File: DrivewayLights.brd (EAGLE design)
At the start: 69.8 x 83.8 mm, 36 parts, among them U1 TLC59108PW

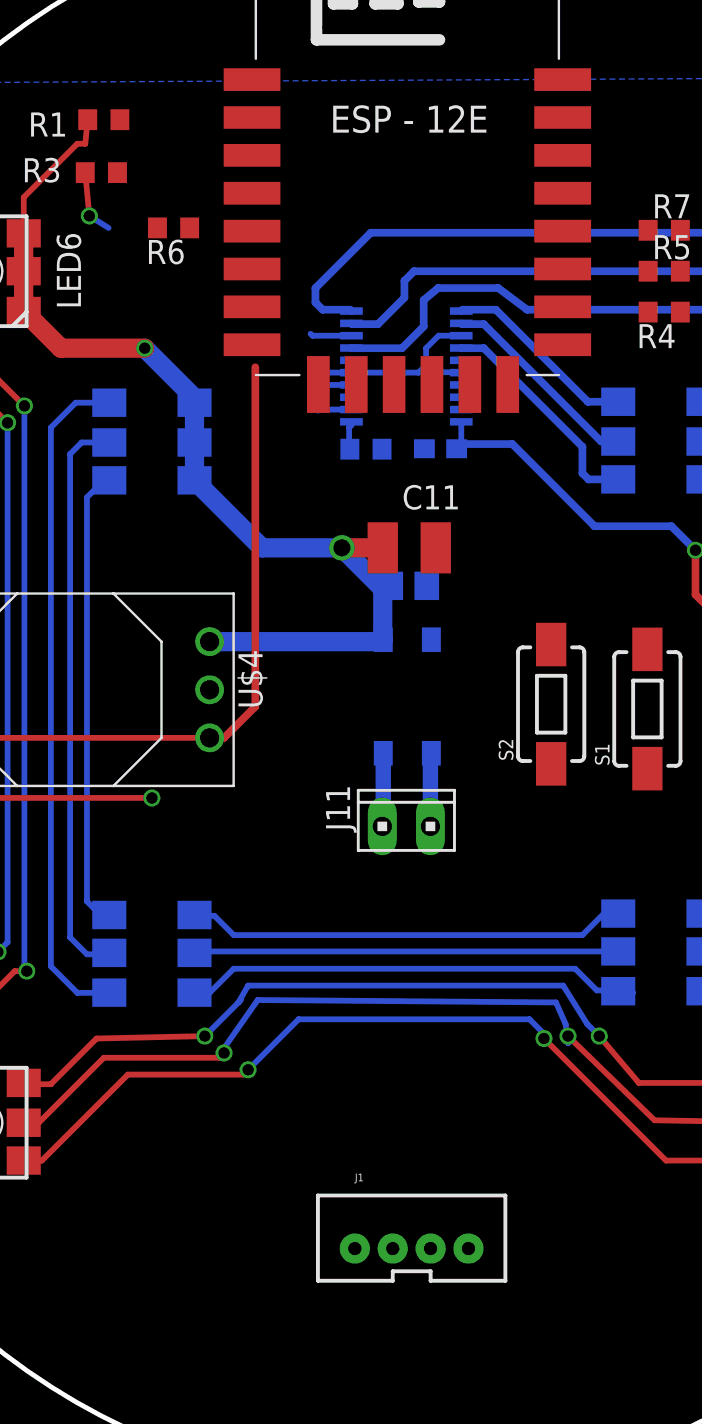
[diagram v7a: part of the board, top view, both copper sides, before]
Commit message: Added some missing connections on schematic and did some more manual routing
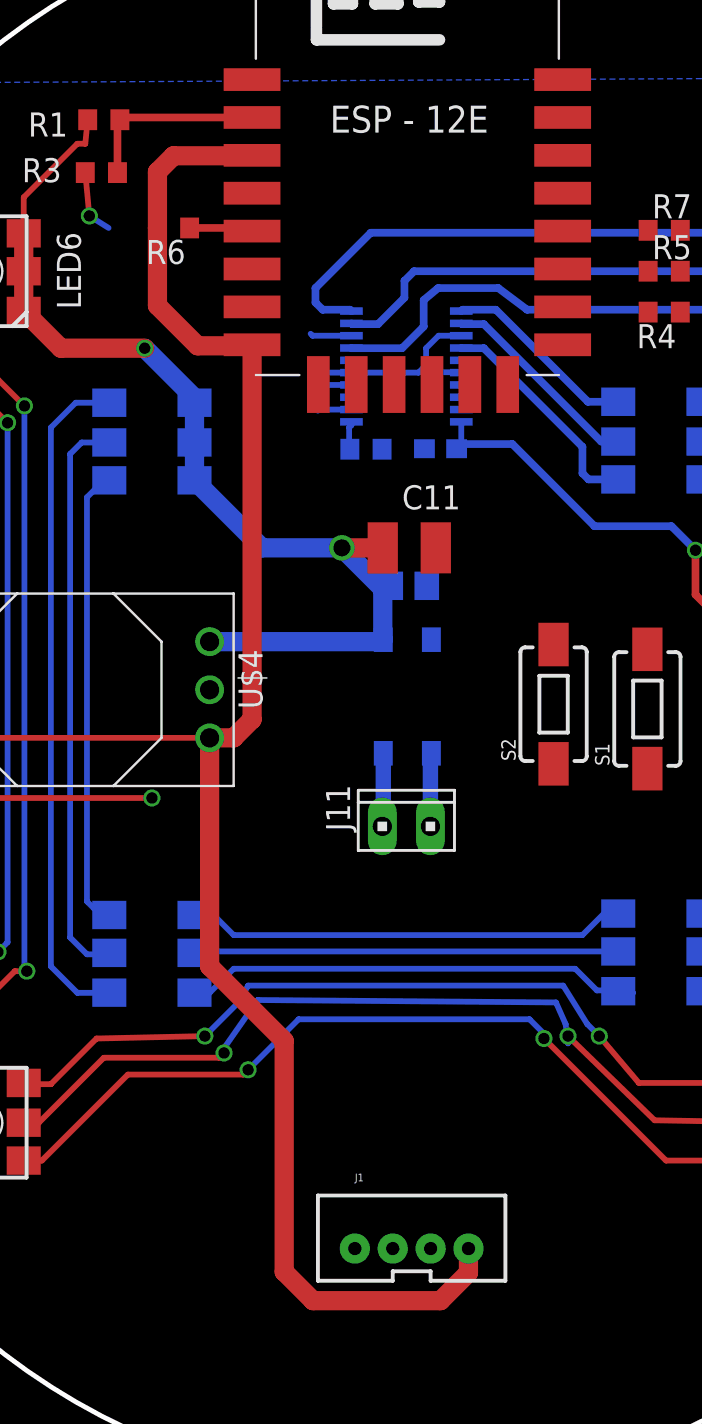
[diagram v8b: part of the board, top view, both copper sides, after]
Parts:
- moved S2 0.13 mm to (42.7, 41.5)
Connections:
- net FLASH_N: now also S1.1
- net GND: now also S1.2, S2.2
- net LED_NRESET: now also U3.GPIO16
- net RESET_N: now also S2.1
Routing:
- net 3.3V: track 105.3 -> 167.1 mm
- net ADC: track 0.00 -> 10.0 mm
- net LED_SCL: track 0.00 -> 3.46 mm
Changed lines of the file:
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@@
 <attribute name="PROD_ID" value="SWCH-00815" x="47.625" y="41.275" size="1.778" layer="27" rot="R90" display="off"/>
 </element>
-<element name="S2" library="SparkFun-Electromechanical" package="TACTILE-SWITCH-1101NE" value="SWITCH-MOMENTARY-2SMD-1101NE" x="42.545" y="41.529" rot="R90">
-<attribute name="PROD_ID" value="SWCH-00815" x="42.545" y="41.529" size="1.778" layer="27" rot="R90" display="off"/>
+<element name="S2" library="SparkFun-Electromechanical" package="TACTILE-SWITCH-1101NE" value="SWITCH-MOMENTARY-2SMD-1101NE" x="42.672" y="41.529" rot="R90">
+<attribute name="PROD_ID" value="SWCH-00815" x="42.672" y="41.529" size="1.778" layer="27" rot="R90" display="off"/>
 </element>
 <element name="J1" library="SparkFun-Connectors" package="JST-4-PTH-VERT" value="" x="35.179" y="13.335">
@@
 <contactref element="R4" pad="1"/>
 <contactref element="J1" pad="1"/>
+<contactref element="S2" pad="2"/>
+<contactref element="S1" pad="2"/>
 <wire x1="43.152" y1="60.507" x2="49.364" y2="62.23" width="0" layer="19" extent="1-1"/>
 <wire x1="37.7996" y1="60.9848" x2="43.152" y2="60.507" width="0" layer="19" extent="1-16"/>
@@
 <wire x1="31.9996" y1="57.0848" x2="31.9996" y2="57.7348" width="0" layer="19" extent="16-16"/>
 <wire x1="29.9472" y1="60.9848" x2="29.972" y2="59.055" width="0" layer="19" extent="16-16"/>
-<wire x1="36.452" y1="49.784" x2="35.9766" y2="47.7774" width="0" layer="19" extent="1-16"/>
+<wire x1="33.616" y1="54.991" x2="31.9996" y2="57.0848" width="0" layer="19" extent="16-16"/>
+<wire x1="35.853" y1="55.0164" x2="33.616" y2="54.991" width="0" layer="19" extent="16-16"/>
+<wire x1="36.452" y1="49.784" x2="35.853" y2="55.0164" width="0" layer="19" extent="1-16"/>
+<wire x1="35.9766" y1="47.7774" x2="36.452" y2="49.784" width="0" layer="19" extent="1-16"/>
+<wire x1="36.2204" y1="44.9354" x2="35.9766" y2="47.7774" width="0" layer="19" extent="16-16"/>
+<wire x1="42.672" y1="44.679" x2="36.2204" y2="44.9354" width="0" layer="19" extent="1-16"/>
+<wire x1="47.625" y1="44.425" x2="42.672" y2="44.679" width="0" layer="19" extent="1-1"/>
+<wire x1="59.436" y1="44.069" x2="47.625" y2="44.425" width="0" layer="19" extent="1-16"/>
+<wire x1="24.511" y1="42.291" x2="36.2204" y2="44.9354" width="0" layer="19" extent="16-16"/>
+<wire x1="21.463" y1="36.576" x2="24.511" y2="42.291" width="0" layer="19" extent="1-1"/>
+<wire x1="19.177" y1="66.675" x2="29.845" y2="61.087" width="0" layer="19" extent="16-16"/>
+<wire x1="32.179" y1="12.785" x2="21.463" y2="36.576" width="0" layer="19" extent="1-1"/>
 </signal>
 <signal name="3.3V">
@@
 <contactref element="IR1A" pad="A"/>
 <contactref element="IR2A" pad="A"/>
-<wire x1="24.511" y1="39.751" x2="25.273" y2="39.751" width="0.4064" layer="1"/>
-<wire x1="25.273" y1="39.751" x2="26.924" y2="41.402" width="0.4064" layer="1"/>
-<wire x1="26.924" y1="41.402" x2="26.924" y2="59.319" width="0.4064" layer="1"/>
 <wire x1="37.7996" y1="56.4348" x2="37.7996" y2="55.263" width="0.3048" layer="16"/>
 <wire x1="37.7996" y1="55.263" x2="37.553" y2="55.0164" width="0.3048" layer="16"/>
@@
 <contactref element="R6" pad="2"/>
 <contactref element="J1" pad="4"/>
+<wire x1="24.511" y1="39.751" x2="24.511" y2="27.686" width="1.016" layer="1"/>
+<wire x1="24.511" y1="27.686" x2="28.448" y2="23.749" width="1.016" layer="1"/>
+<wire x1="28.448" y1="23.749" x2="28.448" y2="11.557" width="1.016" layer="1"/>
+<wire x1="28.448" y1="11.557" x2="29.972" y2="10.033" width="1.016" layer="1"/>
+<wire x1="29.972" y1="10.033" x2="36.703" y2="10.033" width="1.016" layer="1"/>
+<wire x1="36.703" y1="10.033" x2="38.179" y2="11.509" width="1.016" layer="1"/>
+<wire x1="38.179" y1="11.509" x2="38.179" y2="12.785" width="1.016" layer="1"/>
+<wire x1="24.511" y1="39.751" x2="25.781" y2="39.751" width="1.016" layer="1"/>
+<wire x1="25.781" y1="39.751" x2="26.752" y2="40.722" width="1.016" layer="1"/>
+<wire x1="26.752" y1="40.722" x2="26.752" y2="60.507" width="1.016" layer="1"/>
+<wire x1="26.752" y1="60.507" x2="26.697" y2="60.452" width="1.016" layer="1"/>
+<wire x1="26.697" y1="60.452" x2="23.876" y2="60.452" width="1.016" layer="1"/>
+<wire x1="23.876" y1="60.452" x2="21.756" y2="62.572" width="1.016" layer="1"/>
+<wire x1="21.756" y1="62.572" x2="21.756" y2="66.675" width="1.016" layer="1"/>
+<wire x1="26.752" y1="70.507" x2="26.73" y2="70.485" width="1.016" layer="1"/>
+<wire x1="26.73" y1="70.485" x2="22.606" y2="70.485" width="1.016" layer="1"/>
+<wire x1="22.606" y1="70.485" x2="21.756" y2="69.635" width="1.016" layer="1"/>
+<wire x1="21.756" y1="69.635" x2="21.756" y2="66.675" width="1.016" layer="1"/>
 <wire x1="49.364" y1="64.389" x2="49.364" y2="66.548" width="0" layer="19" extent="1-1"/>
 <wire x1="40.495" y1="55.263" x2="49.364" y2="64.389" width="0" layer="19" extent="1-16"/>
-<wire x1="26.924" y1="59.319" x2="37.7996" y2="56.4348" width="0" layer="19" extent="1-16"/>
-<wire x1="26.752" y1="60.507" x2="26.924" y2="59.319" width="0" layer="19" extent="1-1"/>
-<wire x1="21.756" y1="66.675" x2="26.752" y2="60.507" width="0" layer="19" extent="1-1"/>
-<wire x1="26.752" y1="70.507" x2="21.756" y2="66.675" width="0" layer="19" extent="1-1"/>
-<wire x1="38.179" y1="12.785" x2="25.273" y2="39.751" width="0" layer="19" extent="1-1"/>
+<wire x1="26.752" y1="60.507" x2="37.7996" y2="56.4348" width="0" layer="19" extent="1-16"/>
 </signal>
 <signal name="LED_CURRENT_R">
@@
 <contactref element="R6" pad="1"/>
 <wire x1="26.752" y1="66.507" x2="37.7996" y2="57.7348" width="0" layer="19" extent="1-16"/>
-<wire x1="23.456" y1="66.675" x2="26.752" y2="66.507" width="0" layer="19" extent="1-1"/>
+<wire x1="23.456" y1="66.675" x2="26.752" y2="66.675" width="0.4064" layer="1"/>
+<wire x1="26.752" y1="66.675" x2="26.752" y2="66.507" width="0.4064" layer="1"/>
 </signal>
 <signal name="N$2">
@@
 <signal name="LED_NRESET">
 <contactref element="U1" pad="17"/>
+<contactref element="U3" pad="GPIO16"/>
+<wire x1="26.752" y1="68.507" x2="37.7996" y2="58.3848" width="0" layer="19" extent="1-16"/>
 </signal>
 <signal name="N$39">
@@
 <contactref element="U3" pad="GPIO0"/>
 <contactref element="R7" pad="1"/>
+<contactref element="S1" pad="1"/>
 <wire x1="43.152" y1="66.507" x2="47.664" y2="66.548" width="0" layer="19" extent="1-1"/>
+<wire x1="47.625" y1="38.125" x2="47.664" y2="66.548" width="0" layer="19" extent="1-1"/>
 </signal>
 <signal name="RESET_N">
 <contactref element="U3" pad="RESET"/>
+<contactref element="S2" pad="1"/>
+<wire x1="42.672" y1="38.379" x2="26.752" y2="74.507" width="0" layer="19" extent="1-1"/>
 </signal>
 <signal name="ADC">
@@
 <contactref element="R3" pad="2"/>
 <contactref element="R1" pad="1"/>
-<wire x1="19.773" y1="72.39" x2="26.752" y2="72.507" width="0" layer="19" extent="1-1"/>
-<wire x1="19.646" y1="69.596" x2="19.773" y2="72.39" width="0" layer="19" extent="1-1"/>
+<wire x1="26.752" y1="72.507" x2="19.773" y2="72.507" width="0.4064" layer="1"/>
+<wire x1="19.773" y1="72.507" x2="19.773" y2="72.39" width="0.4064" layer="1"/>
+<wire x1="19.773" y1="72.39" x2="19.646" y2="72.39" width="0.4064" layer="1"/>
+<wire x1="19.646" y1="72.39" x2="19.646" y2="69.596" width="0.4064" layer="1"/>
 </signal>
 <signal name="RX">
